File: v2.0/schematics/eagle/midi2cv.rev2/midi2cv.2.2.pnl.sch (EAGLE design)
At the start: 22 parts, among them IC1 TL084P, IC2 TL084P, J1 CV3 OUT, J2 CV2 OUT, J3 CV1 OUT, J4 GATE1 OUT, J5 GATE2 OUT, J6 GATE3 OUT, J7 GATE4 OUT, J8 GATE5 OUT

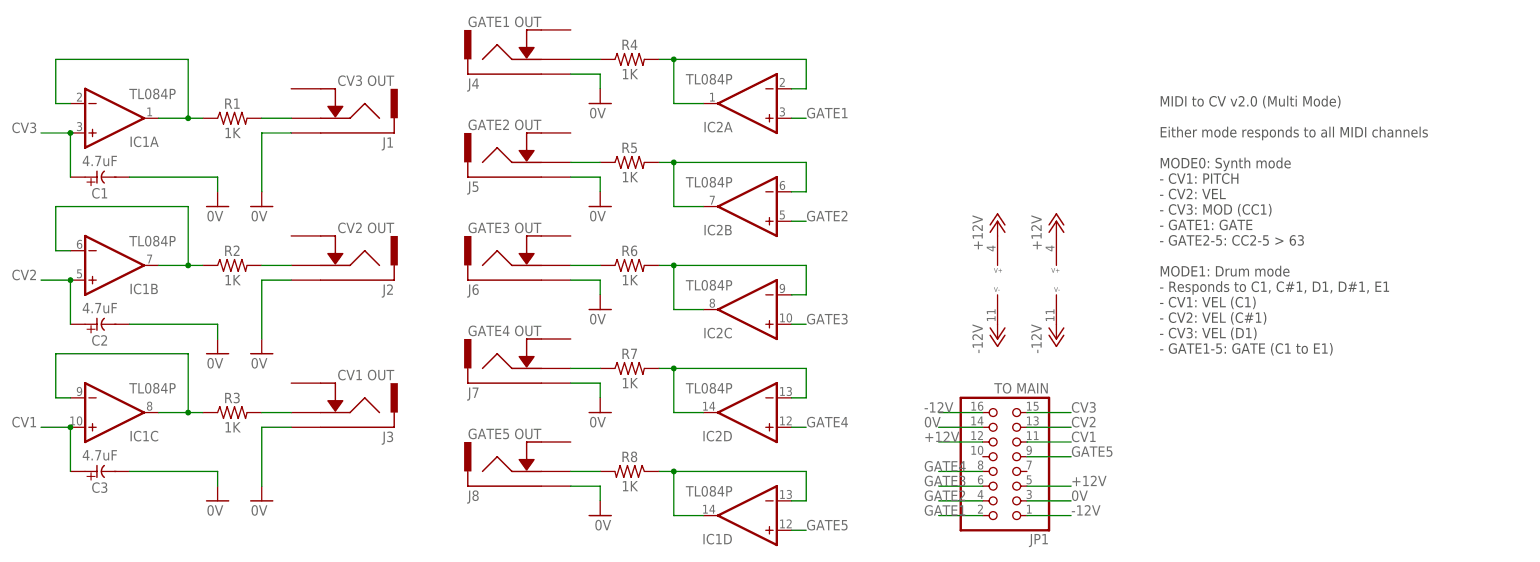
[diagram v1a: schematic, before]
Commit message: Updated version on schem and board to 2.2 Revised labels for GATE1..5 to match board layout and firmare
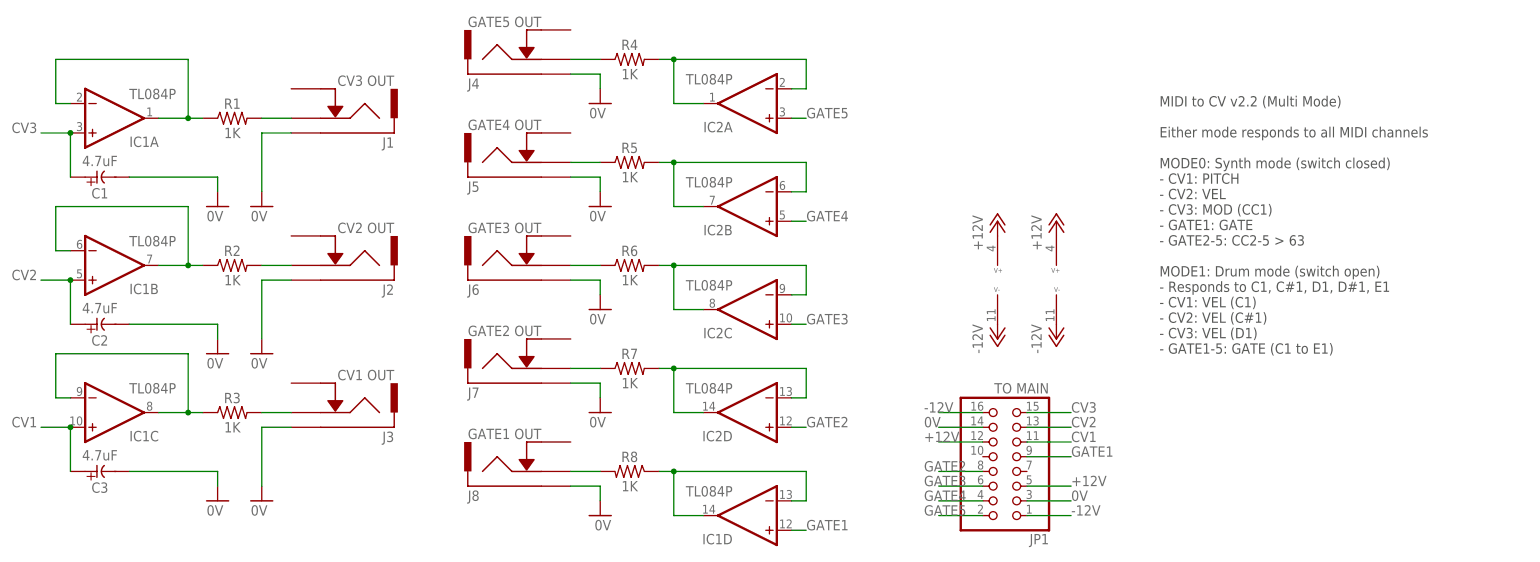
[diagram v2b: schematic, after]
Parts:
- J4: value GATE1 OUT -> GATE5 OUT
- J5: value GATE2 OUT -> GATE4 OUT
- J7: value GATE4 OUT -> GATE2 OUT
- J8: value GATE5 OUT -> GATE1 OUT
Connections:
- net GATE1: now also IC1D.+IN, JP1.9; no longer IC2A.+IN, JP1.2
- net GATE2: now also IC2D.+IN, JP1.8; no longer IC2B.+IN, JP1.4
- net GATE4: now also IC2B.+IN, JP1.4; no longer IC2D.+IN, JP1.8
- net GATE5: now also IC2A.+IN, JP1.2; no longer IC1D.+IN, JP1.9
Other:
- note added: "MIDI to CV v2.2 (Multi Mode) Either mode responds to all MIDI channels MODE0: Synth mode (switch closed) - CV1: PITCH - CV2: VEL - CV3: MOD (CC1) - GATE1: GATE - GATE2-5: CC2-5 > 63 MODE1: Drum mode (switch open) - Responds to C1, C#1, D1, D#1, E1 - CV1: VEL (C1) - CV2: VEL (C#1) - CV3: VEL (D1) - GATE1-5: GATE (C1 to E1)"
- note removed: "MIDI to CV v2.0 (Multi Mode) Either mode responds to all MIDI channels MODE0: Synth mode - CV1: PITCH - CV2: VEL - CV3: MOD (CC1) - GATE1: GATE - GATE2-5: CC2-5 > 63 MODE1: Drum mode - Responds to C1, C#1, D1, D#1, E1 - CV1: VEL (C1) - CV2: VEL (C#1) - CV3: VEL (D1) - GATE1-5: GATE (C1 to E1)"
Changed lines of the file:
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@@
 <?xml version="1.0" encoding="utf-8"?>
 <!DOCTYPE eagle SYSTEM "eagle.dtd">
-<eagle version="7.5.0">
+<eagle version="7.2.0">
 <drawing>
 <settings>
@@
 <part name="R6" library="_common" deviceset="R" device="0309/10" value="1K"/>
 <part name="R7" library="_common" deviceset="R" device="0309/10" value="1K"/>
-<part name="J4" library="jacks" deviceset="ACJM-MV35-2S" device="" value="GATE1 OUT"/>
-<part name="J5" library="jacks" deviceset="ACJM-MV35-2S" device="" value="GATE2 OUT"/>
+<part name="J4" library="jacks" deviceset="ACJM-MV35-2S" device="" value="GATE5 OUT"/>
+<part name="J5" library="jacks" deviceset="ACJM-MV35-2S" device="" value="GATE4 OUT"/>
 <part name="J6" library="jacks" deviceset="ACJM-MV35-2S" device="" value="GATE3 OUT"/>
-<part name="J7" library="jacks" deviceset="ACJM-MV35-2S" device="" value="GATE4 OUT"/>
-<part name="J8" library="jacks" deviceset="ACJM-MV35-2S" device="" value="GATE5 OUT"/>
+<part name="J7" library="jacks" deviceset="ACJM-MV35-2S" device="" value="GATE2 OUT"/>
+<part name="J8" library="jacks" deviceset="ACJM-MV35-2S" device="" value="GATE1 OUT"/>
 <part name="J1" library="jacks" deviceset="ACJM-MV35-2S" device="" value="CV3 OUT"/>
 <part name="J2" library="jacks" deviceset="ACJM-MV35-2S" device="" value="CV2 OUT"/>
@@
 <sheet>
 <plain>
-<text x="142.24" y="66.04" size="1.778" layer="97">MIDI to CV v2.0 (Multi Mode)
+<text x="142.24" y="66.04" size="1.778" layer="97">MIDI to CV v2.2 (Multi Mode)
 Either mode responds to all MIDI channels
-MODE0: Synth mode
+MODE0: Synth mode (switch closed)
 - CV1: PITCH
 - CV2: VEL
@@
 - GATE1: GATE
 - GATE2-5: CC2-5 &gt; 63
-MODE1: Drum mode
+MODE1: Drum mode (switch open)
 - Responds to C1, C#1, D1, D#1, E1
 - CV1: VEL (C1)
@@
 </segment>
 </net>
-<net name="GATE1" class="0">
-<segment>
-<pinref part="JP1" gate="A" pin="2"/>
-<wire x1="111.76" y1="38.1" x2="104.14" y2="38.1" width="0.1524" layer="91"/>
-<label x="101.6" y="38.1" size="1.778" layer="95"/>
-</segment>
-<segment>
-<pinref part="IC2" gate="A" pin="+IN"/>
-<wire x1="78.74" y1="106.68" x2="81.28" y2="106.68" width="0.1524" layer="91"/>
-<label x="81.28" y="106.68" size="1.778" layer="95"/>
-</segment>
-</net>
-<net name="GATE2" class="0">
-<segment>
-<pinref part="JP1" gate="A" pin="4"/>
-<wire x1="111.76" y1="40.64" x2="104.14" y2="40.64" width="0.1524" layer="91"/>
-<label x="101.6" y="40.64" size="1.778" layer="95"/>
-</segment>
-<segment>
-<pinref part="IC2" gate="B" pin="+IN"/>
-<wire x1="78.74" y1="88.9" x2="81.28" y2="88.9" width="0.1524" layer="91"/>
-<label x="81.28" y="88.9" size="1.778" layer="95"/>
-</segment>
-</net>
 <net name="GATE3" class="0">
 <segment>
@@
 <wire x1="78.74" y1="71.12" x2="81.28" y2="71.12" width="0.1524" layer="91"/>
 <label x="81.28" y="71.12" size="1.778" layer="95"/>
-</segment>
-</net>
-<net name="GATE4" class="0">
-<segment>
-<pinref part="JP1" gate="A" pin="8"/>
-<wire x1="111.76" y1="45.72" x2="104.14" y2="45.72" width="0.1524" layer="91"/>
-<label x="101.6" y="45.72" size="1.778" layer="95"/>
-</segment>
-<segment>
-<pinref part="IC2" gate="D" pin="+IN"/>
-<wire x1="78.74" y1="53.34" x2="81.28" y2="53.34" width="0.1524" layer="91"/>
-<label x="81.28" y="53.34" size="1.778" layer="95"/>
-</segment>
-</net>
-<net name="GATE5" class="0">
-<segment>
-<pinref part="JP1" gate="A" pin="9"/>
-<wire x1="119.38" y1="48.26" x2="127" y2="48.26" width="0.1524" layer="91"/>
-<label x="127" y="48.26" size="1.778" layer="95"/>
-</segment>
-<segment>
-<pinref part="IC1" gate="D" pin="+IN"/>
-<wire x1="78.74" y1="35.56" x2="81.28" y2="35.56" width="0.1524" layer="91"/>
-<label x="81.28" y="35.56" size="1.778" layer="95"/>
 </segment>
 </net>
@@
 </segment>
 </net>
+<net name="GATE5" class="0">
+<segment>
+<pinref part="IC2" gate="A" pin="+IN"/>
+<wire x1="78.74" y1="106.68" x2="81.28" y2="106.68" width="0.1524" layer="91"/>
+<label x="81.28" y="106.68" size="1.778" layer="95"/>
+</segment>
+<segment>
+<pinref part="JP1" gate="A" pin="2"/>
+<wire x1="111.76" y1="38.1" x2="104.14" y2="38.1" width="0.1524" layer="91"/>
+<label x="101.6" y="38.1" size="1.778" layer="95"/>
+</segment>
+</net>
+<net name="GATE4" class="0">
+<segment>
+<pinref part="IC2" gate="B" pin="+IN"/>
+<wire x1="78.74" y1="88.9" x2="81.28" y2="88.9" width="0.1524" layer="91"/>
+<label x="81.28" y="88.9" size="1.778" layer="95"/>
+</segment>
+<segment>
+<pinref part="JP1" gate="A" pin="4"/>
+<wire x1="111.76" y1="40.64" x2="104.14" y2="40.64" width="0.1524" layer="91"/>
+<label x="101.6" y="40.64" size="1.778" layer="95"/>
+</segment>
+</net>
+<net name="GATE2" class="0">
+<segment>
+<pinref part="IC2" gate="D" pin="+IN"/>
+<wire x1="78.74" y1="53.34" x2="81.28" y2="53.34" width="0.1524" layer="91"/>
+<label x="81.28" y="53.34" size="1.778" layer="95"/>
+</segment>
+<segment>
+<pinref part="JP1" gate="A" pin="8"/>
+<wire x1="111.76" y1="45.72" x2="104.14" y2="45.72" width="0.1524" layer="91"/>
+<label x="101.6" y="45.72" size="1.778" layer="95"/>
+</segment>
+</net>
+<net name="GATE1" class="0">
+<segment>
+<pinref part="IC1" gate="D" pin="+IN"/>
+<wire x1="78.74" y1="35.56" x2="81.28" y2="35.56" width="0.1524" layer="91"/>
+<label x="81.28" y="35.56" size="1.778" layer="95"/>
+</segment>
+<segment>
+<pinref part="JP1" gate="A" pin="9"/>
+<wire x1="119.38" y1="48.26" x2="127" y2="48.26" width="0.1524" layer="91"/>
+<label x="127" y="48.26" size="1.778" layer="95"/>
+</segment>
+</net>
